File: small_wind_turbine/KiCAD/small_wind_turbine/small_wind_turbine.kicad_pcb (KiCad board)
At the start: 2 copper layers, 90 x 90 mm, 92 parts, among them J1 Conn_01x03_Male, J2 Conn_01x03_Male, J3 Conn_01x03_Male, K1 G5LE-1, Q1 Q_NMOS_GDS, SW1 SW_Push_SPDT, U10 AZ1117-5.0, U2 UC2844A, U3 LTC4440ES6, U4 Opamp_Quad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

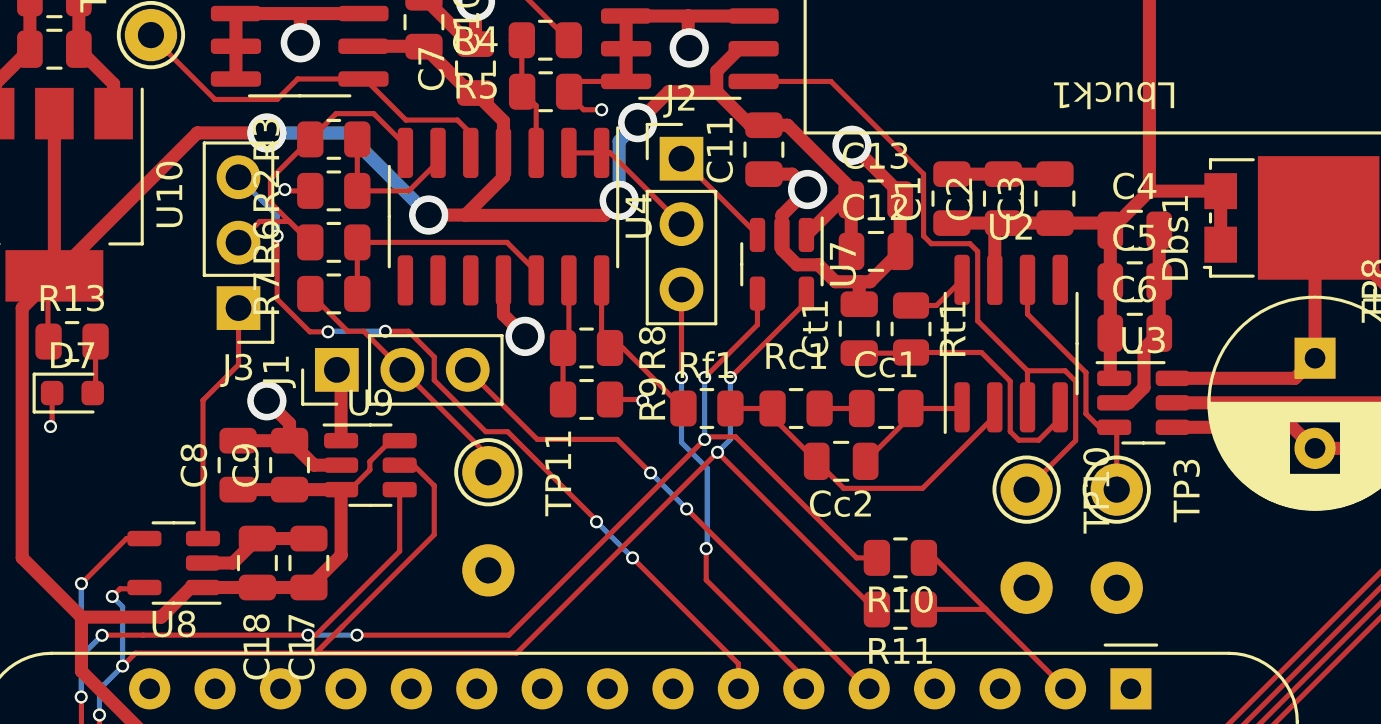
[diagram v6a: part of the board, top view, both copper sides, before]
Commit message: finish connecting ground vias
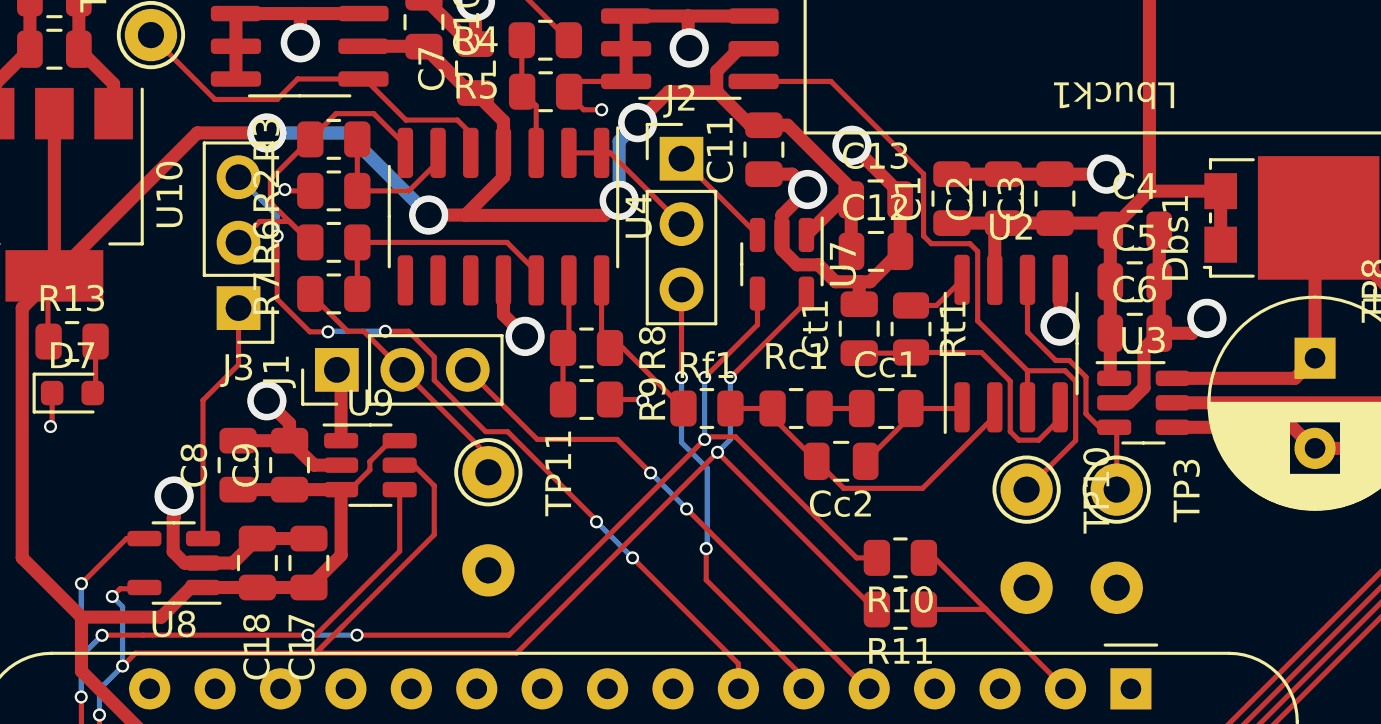
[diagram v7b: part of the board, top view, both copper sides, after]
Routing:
- net GND: track 125.2 -> 134.6 mm, vias 23 -> 27
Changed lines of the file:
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@@
   (segment (start 107.765 56.135) (end 107.8 56.1) (width 0.508) (layer "F.Cu") (net 4))
   (segment (start 47.8 68.75) (end 47.8 70.75) (width 0.508) (layer "F.Cu") (net 4))
+  (segment (start 85.7 77.6) (end 87.7 77.6) (width 0.508) (layer "F.Cu") (net 4))
   (segment (start 68.425 86.35) (end 69.65 86.35) (width 0.2) (layer "F.Cu") (net 4))
   (segment (start 56.7325 91.75) (end 54.7325 91.75) (width 0.508) (layer "F.Cu") (net 4))
+  (segment (start 51.4615 90.9615) (end 51.4615 92.2615) (width 0.508) (layer "F.Cu") (net 4))
   (segment (start 56.535 71.365) (end 56.4 71.5) (width 0.508) (layer "F.Cu") (net 4))
   (segment (start 128.3425 71.535) (end 128.3625 71.555) (width 0.508) (layer "F.Cu") (net 4))
@@
   (segment (start 69.05 72.73) (end 69.05 71.46) (width 0.508) (layer "F.Cu") (net 4))
   (segment (start 78.521 81.779) (end 78.121 81.779) (width 0.508) (layer "F.Cu") (net 4))
+  (segment (start 51.5 90.1) (end 51.5 90.923) (width 0.508) (layer "F.Cu") (net 4))
+  (segment (start 51.5 90.923) (end 51.4615 90.9615) (width 0.508) (layer "F.Cu") (net 4))
   (segment (start 55.9825 87.2825) (end 55.1 86.4) (width 0.508) (layer "F.Cu") (net 4))
   (segment (start 69.05 74) (end 67.2375 74) (width 0.2) (layer "F.Cu") (net 4))
@@
   (segment (start 59.195 54.04) (end 59.195 51.96) (width 0.508) (layer "F.Cu") (net 4))
   (segment (start 69.05 74) (end 69.05 72.73) (width 0.508) (layer "F.Cu") (net 4))
+  (segment (start 51.9 92.7) (end 52.62 92.7) (width 0.508) (layer "F.Cu") (net 4))
   (segment (start 79.69 78.6) (end 79.69 80.59) (width 0.508) (layer "F.Cu") (net 4))
   (segment (start 44.06 57.92) (end 44.04 57.9) (width 0.508) (layer "F.Cu") (net 4))
@@
   (segment (start 123.1875 84.1) (end 125.2 84.1) (width 0.2) (layer "F.Cu") (net 4))
   (segment (start 57.56 51.96) (end 57.5 51.9) (width 0.508) (layer "F.Cu") (net 4))
+  (segment (start 85.905 81.703792) (end 85.905 83.495) (width 0.508) (layer "F.Cu") (net 4))
   (segment (start 89.75 83.778792) (end 89.75 81.778792) (width 0.508) (layer "F.Cu") (net 4))
   (segment (start 89.1585 85.886977) (end 89.1585 84.370292) (width 0.508) (layer "F.Cu") (net 4))
@@
   (segment (start 57.9825 88.9) (end 56.9325 88.9) (width 0.508) (layer "F.Cu") (net 4))
   (segment (start 78.1 82.65) (end 78.1 81.8) (width 0.508) (layer "F.Cu") (net 4))
+  (segment (start 91.021208 83.778792) (end 91.6 83.2) (width 0.508) (layer "F.Cu") (net 4))
   (segment (start 55.85 78.25) (end 56.7875 78.25) (width 0.2) (layer "F.Cu") (net 4))
   (segment (start 46.7625 86.1) (end 46.7625 87.3375) (width 0.2) (layer "F.Cu") (net 4))
@@
   (segment (start 47.8 68.75) (end 47.8 66.9) (width 0.508) (layer "F.Cu") (net 4))
   (segment (start 66.8375 74.5375) (end 67.2 74.9) (width 0.2) (layer "F.Cu") (net 4))
+  (segment (start 89.75 83.778792) (end 91.021208 83.778792) (width 0.508) (layer "F.Cu") (net 4))
   (segment (start 123.1875 81.1) (end 125.2 81.1) (width 0.2) (layer "F.Cu") (net 4))
   (segment (start 77.179 81.779) (end 76.521 81.121) (width 0.508) (layer "F.Cu") (net 4))
   (segment (start 67.2 74.9) (end 67.4 75.1) (width 0.2) (layer "F.Cu") (net 4))
+  (segment (start 85.905 83.495) (end 85.9 83.5) (width 0.508) (layer "F.Cu") (net 4))
   (segment (start 53.9 72.635) (end 53.9 71.365) (width 0.508) (layer "F.Cu") (net 4))
   (segment (start 88 86.478792) (end 88.566685 86.478792) (width 0.508) (layer "F.Cu") (net 4))
+  (segment (start 51.4615 92.2615) (end 51.9 92.7) (width 0.508) (layer "F.Cu") (net 4))
   (segment (start 78.05 82.65) (end 78.1 82.65) (width 0.508) (layer "F.Cu") (net 4))
   (segment (start 59.195 47.34) (end 59.195 45.26) (width 0.508) (layer "F.Cu") (net 4))
@@
   (via (at 71.5 72.7) (size 1.524) (drill 1.016) (layers "F.Cu" "B.Cu") (net 4))
   (via (at 47.8 66.9) (size 1.524) (drill 1.016) (layers "F.Cu" "B.Cu") (net 4))
+  (via (at 87.7 77.6) (size 1.524) (drill 1.016) (layers "F.Cu" "B.Cu") (net 4))
+  (via (at 91.6 83.2) (size 1.524) (drill 1.016) (layers "F.Cu" "B.Cu") (net 4))
+  (via (at 85.9 83.5) (size 1.524) (drill 1.016) (layers "F.Cu" "B.Cu") (net 4))
   (via (at 76.096761 78.196761) (size 1.524) (drill 1.016) (layers "F.Cu" "B.Cu") (net 4))
   (via (at 125.2 81.1) (size 0.508) (drill 0.3302) (layers "F.Cu" "B.Cu") (net 4))
@@
   (via (at 55.1 86.4) (size 1.524) (drill 1.016) (layers "F.Cu" "B.Cu") (net 4))
   (via (at 69.7 86.4) (size 0.508) (drill 0.3302) (layers "F.Cu" "B.Cu") (net 4))
+  (via (at 51.5 90.1) (size 1.524) (drill 1.016) (layers "F.Cu" "B.Cu") (net 4))
   (via (at 57.6 45.2) (size 1.524) (drill 1.016) (layers "F.Cu" "B.Cu") (net 4))
   (via (at 125.2 84.1) (size 0.508) (drill 0.3302) (layers "F.Cu" "B.Cu") (net 4))
@@
   (segment (start 82.7 80.6) (end 82.4 80.3) (width 0.2) (layer "F.Cu") (net 65))
   (segment (start 86.505 85.642396) (end 86.505 87.945) (width 0.2) (layer "F.Cu") (net 65))
-  (segment (start 86.905 86.905) (end 86.905 85.305) (width 0.2) (layer "F.Cu") (net 66))
+  (segment (start 86.905 86.905) (end 86.905 85.47671) (width 0.2) (layer "F.Cu") (net 66))
+  (segment (start 88.1 87.528792) (end 88.1 89.85) (width 0.2) (layer "F.Cu") (net 66))
   (segment (start 88 87.428792) (end 87.428792 87.428792) (width 0.2) (layer "F.Cu") (net 66))
-  (segment (start 88.1 87.528792) (end 88.1 89.85) (width 0.2) (layer "F.Cu") (net 66))
-  (segment (start 84.635 83.035) (end 84.635 81.703792) (width 0.2) (layer "F.Cu") (net 66))
+  (segment (start 86.26329 84.835) (end 85.733105 84.835) (width 0.2) (layer "F.Cu") (net 66))
+  (segment (start 86.905 85.47671) (end 86.26329 84.835) (width 0.2) (layer "F.Cu") (net 66))
   (segment (start 87.428792 87.428792) (end 86.905 86.905) (width 0.2) (layer "F.Cu") (net 66))
   (segment (start 88 87.428792) (end 88.1 87.528792) (width 0.2) (layer "F.Cu") (net 66))
-  (segment (start 86.905 85.305) (end 84.635 83.035) (width 0.2) (layer "F.Cu") (net 66))
+  (segment (start 85.733105 84.835) (end 84.635 83.736895) (width 0.2) (layer "F.Cu") (net 66))
+  (segment (start 84.635 83.736895) (end 84.635 81.703792) (width 0.2) (layer "F.Cu") (net 66))
   (segment (start 58.6125 76.25) (end 58.6125 78.25) (width 0.2) (layer "F.Cu") (net 67))
   (segment (start 61.7475 76.775) (end 61.7475 77.116396) (width 0.2) (layer "F.Cu") (net 67))

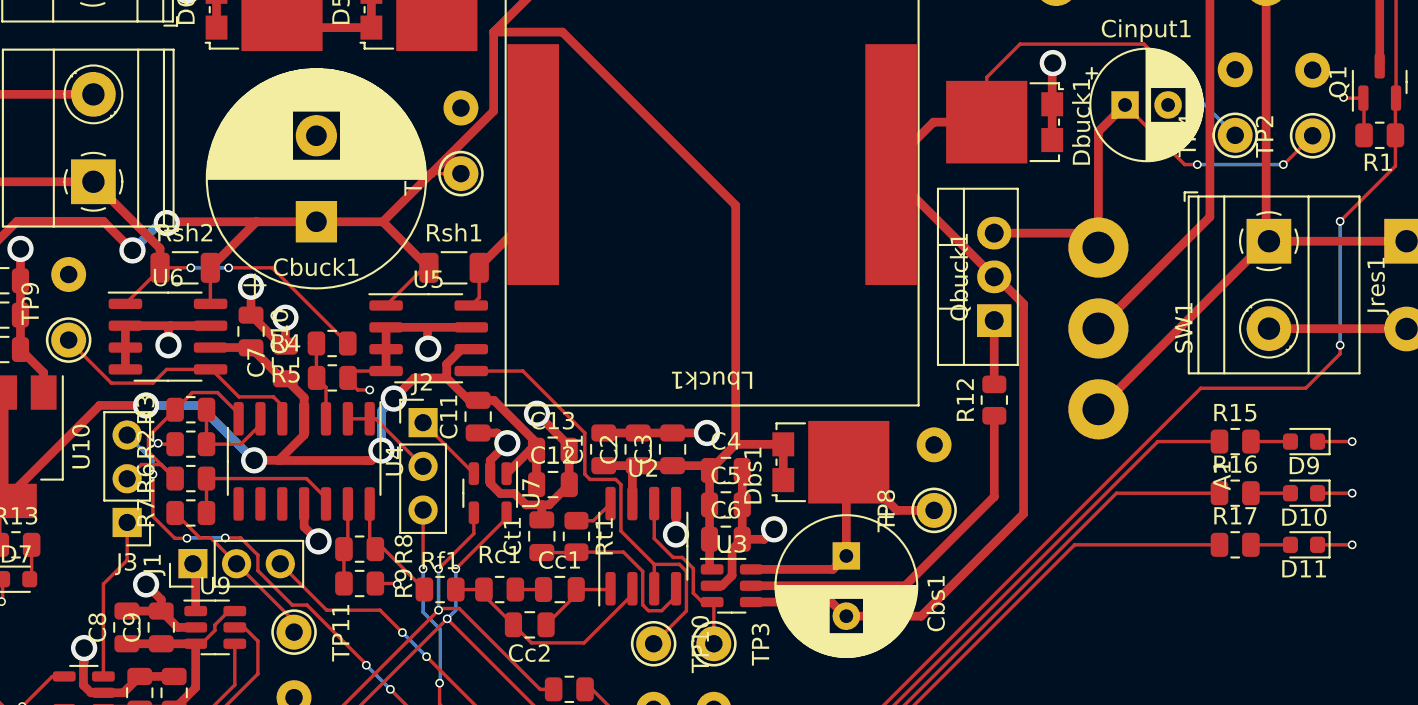
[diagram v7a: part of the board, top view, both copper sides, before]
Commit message: improve ground plane near relay
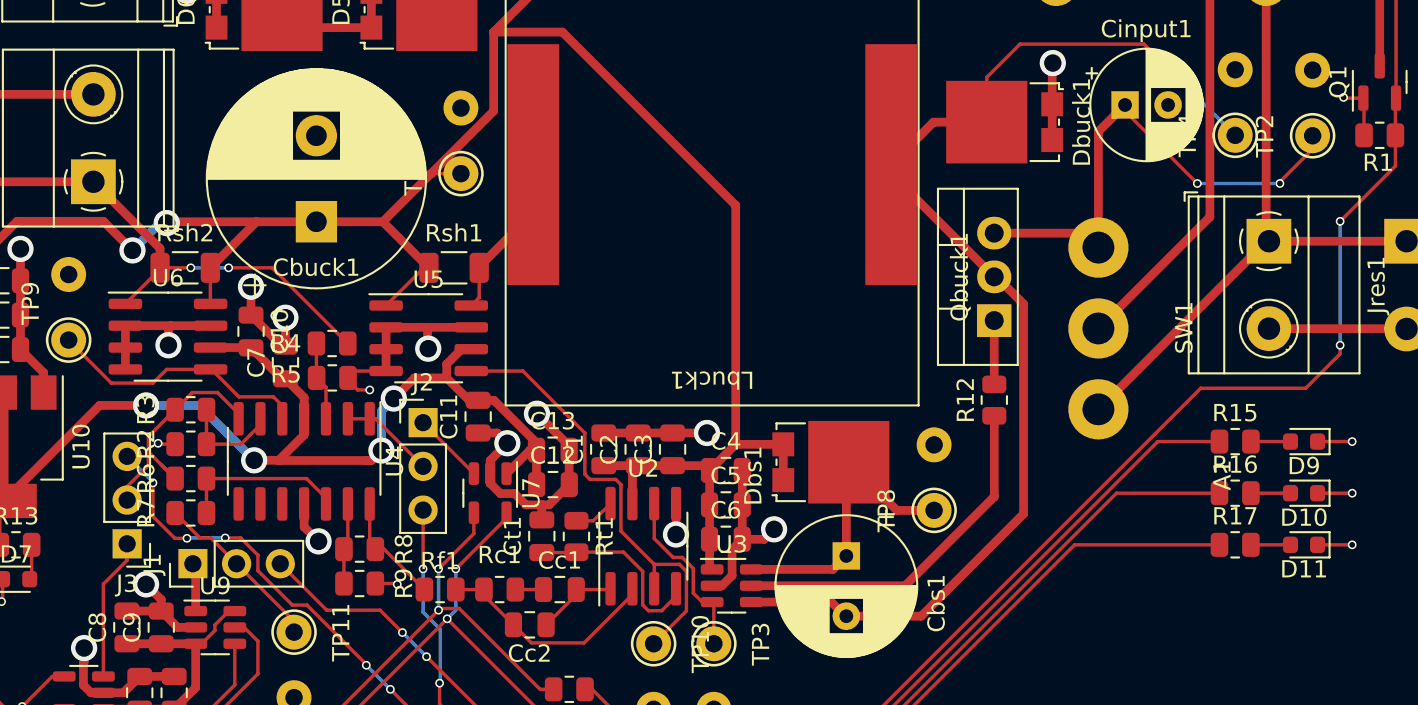
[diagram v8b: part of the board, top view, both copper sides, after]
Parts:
- moved J3 1.24 mm to (54.0, 84.0)
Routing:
- net /RECTIFIER_VDD: track 28.4 -> 30.0 mm
- net Net-(J3-Pad1): track 9.52 -> 8.28 mm
- net /ALTERNATE_ADC_2: track 30.7 -> 29.4 mm
- net Net-(J3-Pad2): track 13.7 -> 14.7 mm
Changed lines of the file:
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@@
   )
   (footprint "Connector_PinHeader_2.54mm:PinHeader_1x03_P2.54mm_Vertical" (layer "F.Cu")
-    (at 54 82.8 180)
+    (at 54 84.04 180)
     (descr "Through hole straight pin header, 1x03, 2.54mm pitch, single row")
     (tags "Through hole pin header THT 1x03 2.54mm single row")
@@
   (segment (start 61.6 85.6) (end 61.6 84.7) (width 0.2) (layer "F.Cu") (net 7))
   (segment (start 61.6 84.7) (end 60.6 83.7) (width 0.2) (layer "F.Cu") (net 7))
-  (segment (start 56.769817 83.722634) (end 55.5 82.452817) (width 0.2) (layer "F.Cu") (net 7))
   (segment (start 73.41 96.61) (end 73.41 97.585) (width 0.2) (layer "F.Cu") (net 7))
-  (segment (start 57.477366 83.722634) (end 56.769817 83.722634) (width 0.2) (layer "F.Cu") (net 7))
+  (segment (start 55.5 82.452817) (end 56.769817 83.722634) (width 0.2) (layer "F.Cu") (net 7))
   (segment (start 63.6 87.6) (end 61.6 85.6) (width 0.2) (layer "F.Cu") (net 7))
   (segment (start 69.3 92.5) (end 73.41 96.61) (width 0.2) (layer "F.Cu") (net 7))
-  (segment (start 55.5 82.452817) (end 55.5 80) (width 0.2) (layer "F.Cu") (net 7))
+  (segment (start 55.5 80.5) (end 55.5 82.452817) (width 0.2) (layer "F.Cu") (net 7))
   (segment (start 60.6 83.7) (end 59.7 83.7) (width 0.2) (layer "F.Cu") (net 7))
   (segment (start 64.45 87.6) (end 63.6 87.6) (width 0.2) (layer "F.Cu") (net 7))
   (segment (start 67.9 91.05) (end 64.45 87.6) (width 0.2) (layer "F.Cu") (net 7))
   (segment (start 67.9 91.1) (end 67.9 91.05) (width 0.2) (layer "F.Cu") (net 7))
+  (segment (start 56.769817 83.722634) (end 57.477366 83.722634) (width 0.2) (layer "F.Cu") (net 7))
   (via (at 67.9 91.1) (size 0.508) (drill 0.3302) (layers "F.Cu" "B.Cu") (net 7))
-  (via (at 55.5 80) (size 0.508) (drill 0.3302) (layers "F.Cu" "B.Cu") (net 7))
+  (via (at 55.5 80.5) (size 0.508) (drill 0.3302) (layers "F.Cu" "B.Cu") (net 7))
   (via (at 69.3 92.5) (size 0.508) (drill 0.3302) (layers "F.Cu" "B.Cu") (net 7))
   (via (at 59.7 83.7) (size 0.508) (drill 0.3302) (layers "F.Cu" "B.Cu") (net 7))
   (via (at 57.477366 83.722634) (size 0.508) (drill 0.3302) (layers "F.Cu" "B.Cu") (net 7))
-  (segment (start 55.5 80) (end 55.5 79.22) (width 0.2) (layer "B.Cu") (net 7))
+  (segment (start 55.5 80.5) (end 55.5 80.46) (width 0.2) (layer "B.Cu") (net 7))
   (segment (start 69.3 92.5) (end 67.9 91.1) (width 0.2) (layer "B.Cu") (net 7))
   (segment (start 57.477366 83.722634) (end 57.5 83.7) (width 0.2) (layer "B.Cu") (net 7))
-  (segment (start 55.5 79.22) (end 54 77.72) (width 0.2) (layer "B.Cu") (net 7))
   (segment (start 57.5 83.7) (end 59.7 83.7) (width 0.2) (layer "B.Cu") (net 7))
+  (segment (start 55.5 80.46) (end 54 78.96) (width 0.2) (layer "B.Cu") (net 7))
   (segment (start 78 92.5) (end 78.7875 92.5) (width 0.2) (layer "F.Cu") (net 16))
   (segment (start 72.1 85.5) (end 74.15 83.45) (width 0.2) (layer "F.Cu") (net 16))
@@
   (segment (start 74.7375 87.0375) (end 76.45 88.75) (width 0.2) (layer "F.Cu") (net 33))
   (segment (start 73.1 86.7) (end 74.7375 86.7) (width 0.2) (layer "F.Cu") (net 33))
-  (segment (start 112 58.535) (end 115.465 62) (width 0.2) (layer "F.Cu") (net 34))
+  (segment (start 121 63.1) (end 121 63) (width 0.2) (layer "F.Cu") (net 34))
+  (segment (start 122.9 61.1) (end 122.9 60.325) (width 0.2) (layer "F.Cu") (net 34))
   (segment (start 109.61 65.985) (end 110.45 66.825) (width 0.508) (layer "F.Cu") (net 34))
-  (segment (start 115.465 62) (end 116.2 62) (width 0.2) (layer "F.Cu") (net 34))
+  (segment (start 116.2 63.1) (end 112 58.9) (width 0.2) (layer "F.Cu") (net 34))
   (segment (start 104.395 65.985) (end 109.61 65.985) (width 0.508) (layer "F.Cu") (net 34))
-  (segment (start 121.225 62) (end 122.9 60.325) (width 0.2) (layer "F.Cu") (net 34))
   (segment (start 110.45 66.825) (end 110.45 60.085) (width 0.508) (layer "F.Cu") (net 34))
   (segment (start 110.45 60.085) (end 112 58.535) (width 0.508) (layer "F.Cu") (net 34))
-  (segment (start 121.2 62) (end 121.225 62) (width 0.2) (layer "F.Cu") (net 34))
-  (via (at 121.2 62) (size 0.508) (drill 0.3302) (layers "F.Cu" "B.Cu") (net 34))
-  (via (at 116.2 62) (size 0.508) (drill 0.3302) (layers "F.Cu" "B.Cu") (net 34))
-  (segment (start 116.2 62) (end 121.2 62) (width 0.2) (layer "B.Cu") (net 34))
+  (segment (start 112 58.9) (end 112 58.535) (width 0.2) (layer "F.Cu") (net 34))
+  (segment (start 121 63) (end 122.9 61.1) (width 0.2) (layer "F.Cu") (net 34))
+  (via (at 121 63.1) (size 0.508) (drill 0.3302) (layers "F.Cu" "B.Cu") (net 34))
+  (via (at 116.2 63.1) (size 0.508) (drill 0.3302) (layers "F.Cu" "B.Cu") (net 34))
+  (segment (start 121 63.1) (end 116.2 63.1) (width 0.2) (layer "B.Cu") (net 34))
   (segment (start 85.905 86.653792) (end 85.905 87.095) (width 0.2) (layer "F.Cu") (net 35))
   (segment (start 82.847604 84.525) (end 80.1125 84.525) (width 0.2) (layer "F.Cu") (net 35))
@@
   (segment (start 54 85) (end 52.62 86.38) (width 0.2) (layer "F.Cu") (net 51))
   (segment (start 52.62 86.38) (end 52.62 91.75) (width 0.2) (layer "F.Cu") (net 51))
-  (segment (start 54 82.8) (end 54 85) (width 0.2) (layer "F.Cu") (net 51))
+  (segment (start 54 85) (end 54 84.04) (width 0.2) (layer "F.Cu") (net 51))
   (segment (start 60.4775 76.4775) (end 59.25 75.25) (width 0.2) (layer "F.Cu") (net 52))
-  (segment (start 54.8225 79.4375) (end 54 80.26) (width 0.2) (layer "F.Cu") (net 52))
   (segment (start 56.7875 76.25) (end 55.2375 77.8) (width 0.2) (layer "F.Cu") (net 52))
+  (segment (start 54 80.716525) (end 54 81.5) (width 0.2) (layer "F.Cu") (net 52))
   (segment (start 56.7875 80.25) (end 55.2375 78.7) (width 0.2) (layer "F.Cu") (net 52))
   (segment (start 60.4775 76.775) (end 60.4775 76.4775) (width 0.2) (layer "F.Cu") (net 52))
-  (segment (start 55.975 79.4375) (end 55.2375 79.4375) (width 0.2) (layer "F.Cu") (net 52))
   (segment (start 57.7875 75.25) (end 56.7875 76.25) (width 0.2) (layer "F.Cu") (net 52))
   (segment (start 59.25 75.25) (end 57.7875 75.25) (width 0.2) (layer "F.Cu") (net 52))
+  (segment (start 55.2375 78.7) (end 55.2375 79.479025) (width 0.2) (layer "F.Cu") (net 52))
   (segment (start 55.975 79.4375) (end 56.7875 80.25) (width 0.2) (layer "F.Cu") (net 52))
-  (segment (start 55.2375 79.4375) (end 54.8225 79.4375) (width 0.2) (layer "F.Cu") (net 52))
+  (segment (start 55.2375 79.479025) (end 54 80.716525) (width 0.2) (layer "F.Cu") (net 52))
   (segment (start 55.2375 78.7) (end 55.2375 77.8) (width 0.2) (layer "F.Cu") (net 52))
   (segment (start 59.9 68) (end 62.425 68) (width 0.2) (layer "F.Cu") (net 53))
